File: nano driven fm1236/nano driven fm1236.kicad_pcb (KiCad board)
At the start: 2 copper layers, 183.5 x 74.3 mm, 68 parts, among them J1 SPI, J2 address select, J3 Left, J4 Right, J5 SJ1-3525N, J6 AF, J7 2nd IF, J8 CVBS, SW1 Up, SW2 Down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

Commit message: made gerbers and added gitignore for kicad
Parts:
- added C19: 220uF, Capacitor_THT:CP_Radial_D5.0mm_P2.50mm, F.Cu at (183.5, 72.9)
- added J9: Barrel_Jack_Switch, Connector_BarrelJack:BarrelJack_Horizontal, F.Cu at (183.2, 67.8)
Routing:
- net +5V: track 220.9 -> 236.6 mm
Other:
- board text added: "5v"

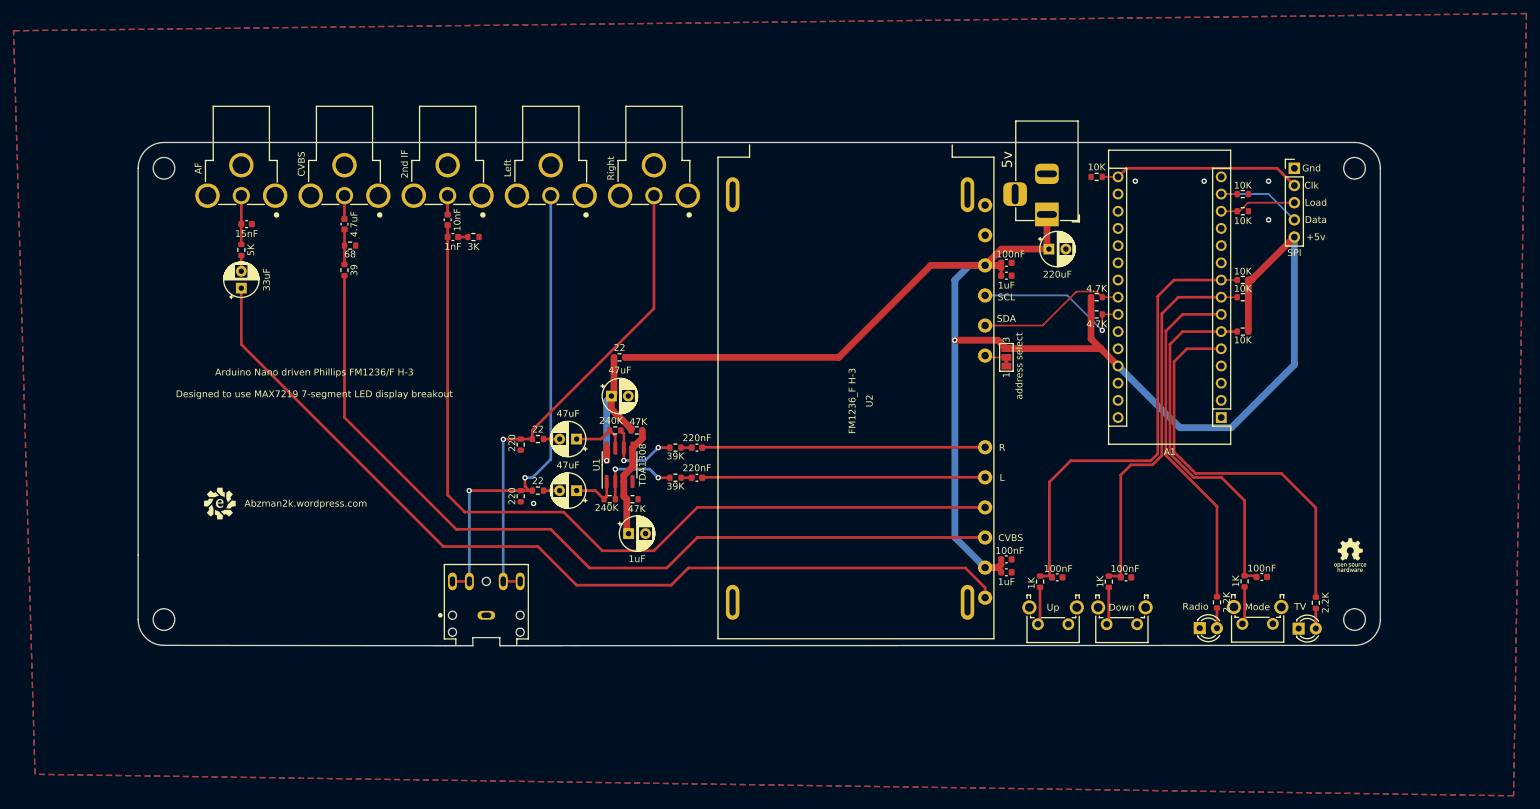
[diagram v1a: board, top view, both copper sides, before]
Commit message: added datasheet(s) notes and example for running the 7-segments
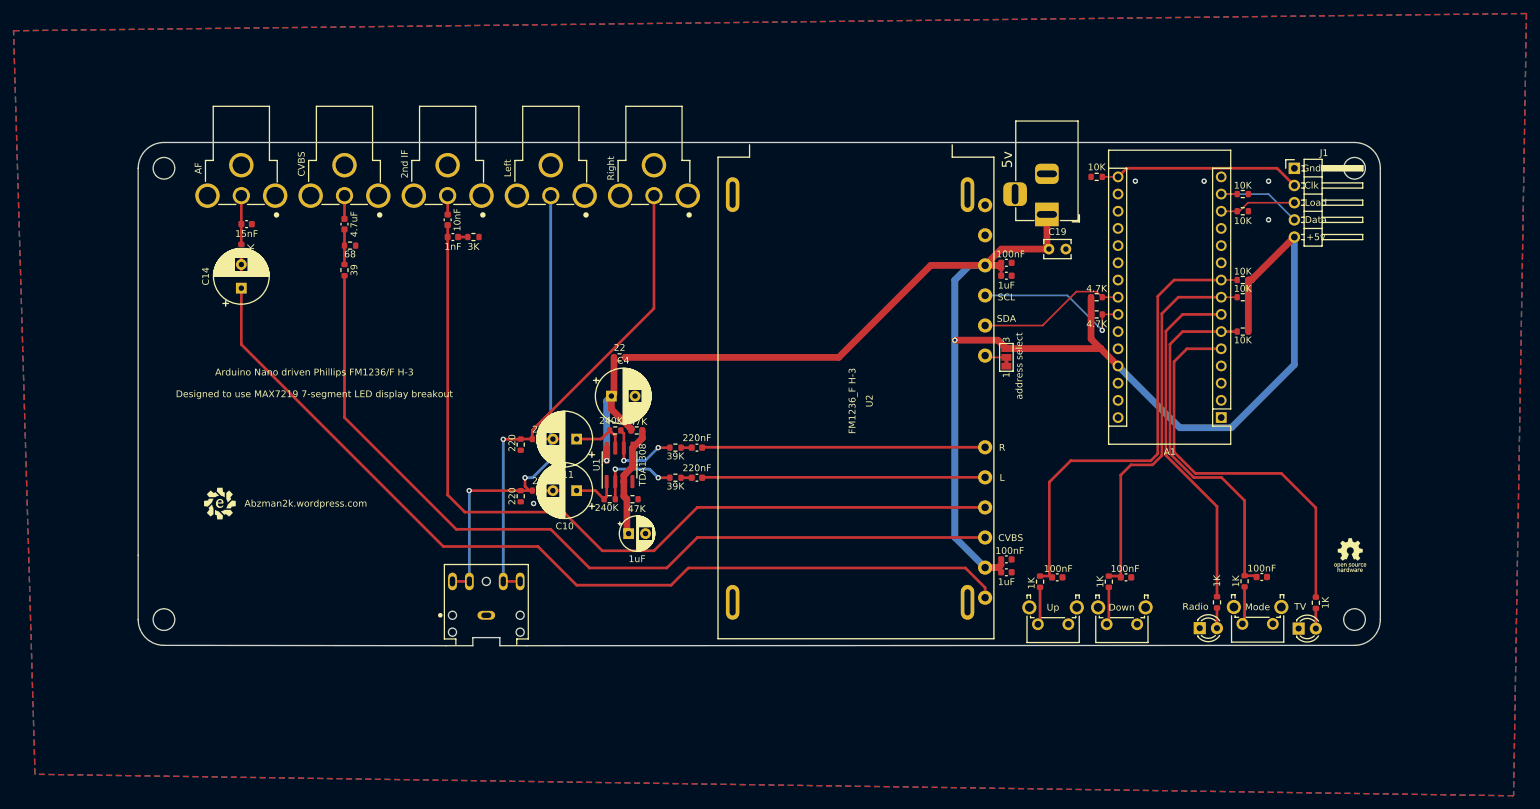
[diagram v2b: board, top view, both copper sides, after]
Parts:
- C10, C11, C14, C4: footprint Capacitor_THT:CP_Radial_D5.0mm_P2.50mm -> Capacitor_THT:CP_Radial_D8.0mm_P3.50mm
- C19: footprint Capacitor_THT:CP_Radial_D5.0mm_P2.50mm -> Capacitor_THT:C_Disc_D3.8mm_W2.6mm_P2.50mm
- J1: footprint Connector_PinHeader_2.54mm:PinHeader_1x05_P2.54mm_Vertical -> Connector_PinHeader_2.54mm:PinHeader_1x05_P2.54mm_Horizontal
- R8, R9: value 2.2K -> 1K
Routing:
- net Net-(J3-Pad2): track 71.3 -> 73.7 mm
- net Net-(C11-Pad2): track 2.39 -> 0.00 mm
